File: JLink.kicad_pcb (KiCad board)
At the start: 2 copper layers, 1 part

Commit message: 20250630
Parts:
- added C1: ~, kicad_community_lib:CL10C200JB81PNC, F.Cu at (157.5, 57.7)
- added C10: 4.7uf, kicad_community_lib:CC0603KRX5R8BB475, F.Cu at (143.0, 83.2)
- added C11: 100nf, kicad_community_lib:0603B104K101CT, F.Cu at (143.0, 85.5)
- added C12: 4.7uf, kicad_community_lib:CC0603KRX5R8BB475, F.Cu at (143.0, 87.9)
- added C13: ~, kicad_community_lib:0603B105K250NT, F.Cu at (143.0, 90.2)
- added C14: ~, kicad_community_lib:0603B105K250NT, F.Cu at (143.0, 92.6)
- added C2: ~, kicad_community_lib:CL10C200JB81PNC, F.Cu at (157.5, 60.1)
- added C3: 10nf, kicad_community_lib:CC0603KRX7R6BB103, F.Cu at (121.0, 82.1)
- added C4: ~, kicad_community_lib:CC0603KRX7R6BB103, F.Cu at (121.0, 84.5)
- added C5: ~, kicad_community_lib:CC0603KRX7R6BB103, F.Cu at (121.0, 86.9)
- added C6: ~, kicad_community_lib:CC0603KRX7R6BB103, F.Cu at (121.0, 89.2)
- added C7: 100nf, kicad_community_lib:0603B104K101CT, F.Cu at (136.8, 57.7)
- added C8: 100nf, kicad_community_lib:0603B104K101CT, F.Cu at (136.8, 60.1)
- added C9: 100nf, kicad_community_lib:0603B104K101CT, F.Cu at (143.0, 80.8)
- added CN1: ~, kicad_community_lib:A2541WV-2x4P, F.Cu at (146.7, 74.3)
- added D1: ~, kicad_community_lib:PRTR5V0U2X__NXP Semiconductors, F.Cu at (136.7, 63.5)
- added LDO1: ~, kicad_community_lib:ME6211C33M5G-N, F.Cu at (146.8, 89.4)
- added R1: ~, kicad_community_lib:RTT03512JTP, F.Cu at (121.0, 57.7)
- added R2: ~, kicad_community_lib:RTT03512JTP, F.Cu at (121.0, 60.1)
- added R3: ~, kicad_community_lib:RC0603FR-0724RL, F.Cu at (121.0, 62.4)
- added R4: ~, kicad_community_lib:RC0603FR-0724RL, F.Cu at (121.0, 64.8)
- added R5: ~, kicad_community_lib:RC0603FR-0724RL, F.Cu at (121.0, 67.2)
- added R6: ~, kicad_community_lib:RC0603FR-0724RL, F.Cu at (121.0, 69.5)
- added RN1: 10K, kicad_community_lib:4D03WGJ0472T5E, F.Cu at (139.0, 67.2)
- added RN2: 10K, kicad_community_lib:4D03WGJ0472T5E, F.Cu at (125.0, 87.0)
- added U2: ~, kicad_community_lib:STM32F205RET6, F.Cu at (148.0, 63.8)
- added U3: ~, kicad_community_lib:B0505S-1W__Rlt, F.Cu at (151.2, 85.5)
- added USB1: TYPE-C 16P CB0.8 073, Connect:USB-C-SMD_TYPE-C-16P-CB0.8-073, F.Cu at (129.4, 73.6)
- added X1: ~, Oscillator:CRYSTAL-SMD_4P-L3.2-W2.5-BL, F.Cu at (155.4, 73.2)
- U1: footprint IC:QFP50P1600X1600X160-100N -> kicad_community_lib:ADUM3160BRWZ-RL
- moved U1 28.4 mm to (128.6, 63.0)
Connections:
- U1 pad 1: unconnected-(U1-PE2-Pad1) -> P5VP
- U1 pad 10: Net-(U1-VSS-Pad10) -> Net-(U1-DD+)
- U1 pad 11: Net-(U1-VDD-Pad100) -> Net-(U1-DD-)
- U1 pad 12: unconnected-(U1-PH0_OSC_IN-Pad12) -> /USB/VDD2
- U1 pad 13: unconnected-(U1-PH1_OSC_OUT-Pad13) -> /USB/VDD2
- U1 pad 14: unconnected-(U1-NRST-Pad14) -> /USB/VDD2
- U1 pad 15: unconnected-(U1-PC0-Pad15) -> GND
- U1 pad 16: unconnected-(U1-PC1-Pad16) -> /USB/P5V
- U1 pad 2: unconnected-(U1-PE3-Pad2) -> PGND
- U1 pad 3: unconnected-(U1-PE4-Pad3) -> /USB/VDD1
- U1 pad 4: unconnected-(U1-PE5-Pad4) -> /USB/VDD1
- U1 pad 5: unconnected-(U1-PE6-Pad5) -> /USB/VDD1
- U1 pad 6: unconnected-(U1-VBAT-Pad6) -> Net-(U1-UD–)
- U1 pad 7: unconnected-(U1-PC13-Pad7) -> Net-(U1-UD+)
- U1 pad 8: unconnected-(U1-PC14_OSC32_IN-Pad8) -> PGND
- U1 pad 9: unconnected-(U1-PC15_OSC32_OUT-Pad9) -> GND

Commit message: 基本完成
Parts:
- added C15: ~, kicad_community_lib:CL10B104KC8NNNC, F.Cu at (86.8, 86.8)
- added C16: ~, kicad_community_lib:CL10B104KC8NNNC, F.Cu at (86.8, 82.8)
- added C17: ~, kicad_community_lib:CL10B104KC8NNNC, F.Cu at (86.8, 78.8)
- added C18: ~, kicad_community_lib:CL10B104KC8NNNC, F.Cu at (86.8, 74.8)
- added C19: ~, kicad_community_lib:CL10B104KC8NNNC, F.Cu at (86.7, 70.8)
- added C20: ~, kicad_community_lib:CL10B104KC8NNNC, F.Cu at (86.8, 66.8)
- added C21: ~, kicad_community_lib:CL10B104KC8NNNC, F.Cu at (86.8, 62.8)
- added C22: ~, kicad_community_lib:CL10B104KC8NNNC, F.Cu at (89.5, 66.8)
- added C23: ~, kicad_community_lib:CL10B104KC8NNNC, F.Cu at (89.5, 62.8)
- added C24: ~, kicad_community_lib:CL10B104KC8NNNC, F.Cu at (89.5, 70.8)
- added C25: ~, kicad_community_lib:CL10B104KC8NNNC, F.Cu at (89.5, 86.8)
- added C26: ~, kicad_community_lib:CL10B104KC8NNNC, F.Cu at (89.5, 82.8)
- added C27: ~, kicad_community_lib:CL10B104KC8NNNC, F.Cu at (89.5, 78.8)
- added C28: ~, kicad_community_lib:CL10B104KC8NNNC, F.Cu at (89.5, 74.8)
- added C29: ~, kicad_community_lib:0603B225K250NT, F.Cu at (77.4, 72.0)
- added C30: ~, kicad_community_lib:0603B225K250NT, B.Cu at (65.5, 72.6)
- added C31: ~, kicad_community_lib:0603B225K250NT, B.Cu at (64.2, 72.6)
- added C32: ~, kicad_community_lib:0603B225K250NT, B.Cu at (67.5, 78.6)
- added C33: ~, kicad_community_lib:0603B225K250NT, F.Cu at (63.5, 83.8)
- added C34: ~, kicad_community_lib:0603B225K250NT, B.Cu at (71.2, 71.8)
- added C35: ~, kicad_community_lib:0603B225K250NT, B.Cu at (70.0, 79.3)
- added C36: ~, kicad_community_lib:0603B225K250NT, B.Cu at (71.2, 78.1)
- added D2: ~, kicad_community_lib:MBR0530__YANGJIE, F.Cu at (69.9, 66.0)
- added D3: ~, kicad_community_lib:MBR0530__YANGJIE, F.Cu at (58.4, 66.2)
- added H1: ~, Connect:PZ200-2-10-Z, F.Cu at (97.9, 75.5)
- added LED1: ~, kicad_community_lib:SZYY0603RB2, F.Cu at (80.4, 71.5)
- added Q1: ~, kicad_community_lib:SS8050__SHIKUES, F.Cu at (76.9, 86.8)
- added Q2: ~, kicad_community_lib:SS8550 Y2, F.Cu at (77.9, 83.0)
- added R7: ~, kicad_community_lib:RK73Z1JTTD, F.Cu at (75.1, 82.5)
- added RN10: 100 Ohm, kicad_community_lib:YC164-FR-07100RL, F.Cu at (93.5, 85.8)
- added RN11: 220K, kicad_community_lib:4D03WGJ0224T5E, F.Cu at (93.3, 77.4)
- added RN3: 10K, kicad_community_lib:4D03WGJ0472T5E, F.Cu at (80.4, 67.8)
- added RN4: 220K, kicad_community_lib:4D03WGJ0224T5E, F.Cu at (93.3, 73.6)
- added RN5: 470Ω, kicad_community_lib:4D03WGJ0471T5E, F.Cu at (93.3, 66.2)
- added RN6: 470Ω, kicad_community_lib:4D03WGJ0471T5E, F.Cu at (93.5, 81.5)
- added RN7: ~, kicad_community_lib:YC164-FR-07100RL, F.Cu at (93.3, 69.9)
- added RN8: 470Ω, kicad_community_lib:4D03WGJ0471T5E, F.Cu at (82.4, 74.8)
- added RN9: 470Ω, kicad_community_lib:4D03WGJ0471T5E, F.Cu at (82.4, 78.8)
- added U10: ~, kicad_community_lib:SN74LVC2T45DCUR, F.Cu at (88.0, 84.8)
- added U11: ~, kicad_community_lib:SN74LVC2T45DCUR, F.Cu at (88.0, 88.8)
- added U4: ~, kicad_community_lib:SN74LVC2T45DCUR, F.Cu at (88.0, 64.8)
- added U5: ~, kicad_community_lib:SN74LVC2T45DCUR, F.Cu at (88.0, 68.8)
- added U6: ~, kicad_community_lib:SN74LVC2T45DCUR, F.Cu at (88.0, 80.8)
- added U7: ~, kicad_community_lib:MCP6002T-I_SN, F.Cu at (64.1, 64.8)
- added U8: ~, kicad_community_lib:SN74LVC2T45DCUR, F.Cu at (88.0, 72.8)
- added U9: ~, kicad_community_lib:SN74LVC2T45DCUR, F.Cu at (88.0, 76.8)
- R3, R4: value ~ -> 24Ω
- moved U3 102.3 mm to (50.6, 66.8)
- moved D1 97.3 mm to (41.5, 83.8), turned to 90 degrees
- moved C9 97.1 mm to (46.6, 69.0), turned to 180 degrees
- moved C1 95.8 mm to (65.5, 84.5), turned to 180 degrees
- moved C10 94.7 mm to (49.4, 69.0), turned to 180 degrees
- moved CN1 92.9 mm to (54.5, 85.8), turned to 180 degrees
- moved C8 92.8 mm to (44.7, 72.0), turned to 90 degrees
- moved C2 92.6 mm to (68.2, 84.5), turned to 180 degrees
- moved C11 91.6 mm to (52.9, 69.0), turned to 180 degrees
- moved USB1 89.9 mm to (39.5, 75.2), turned to -90 degrees
- moved X1 89.8 mm to (66.7, 87.3), turned to 180 degrees
- moved C12 89.6 mm to (55.4, 69.0)
- moved R2 86.0 mm to (38.3, 83.2), turned to 180 degrees
- moved R1 83.2 mm to (38.5, 67.8), turned to 180 degrees
- moved U2 80.7 mm to (68.1, 75.5), turned to 90 degrees
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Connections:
- net /Connect/TIMA renamed TIMA
- net /STM32/JTCK_SWCK renamed JTCK_SWCK
- net /STM32/JTCK_SWDIO renamed JTCK_SWDIO
- net /STM32/JTDI renamed JTDI
- net /STM32/JTDO_SWO renamed JTDO_SWO
- net /STM32/JTRST renamed JTRST
- R3 pad 1: /USB/PDD_P -> /PDDP
- R4 pad 1: /USB/PDD_N -> /PDDM
- RN2 pad 1: /Connect/PADC1 -> /ADC4
- RN2 pad 2: /Connect/PADC2 -> /ADC3
- RN2 pad 3: /Connect/PADC3 -> /ADC2
- RN2 pad 4: /Connect/PADC4 -> /ADC1
- RN2 pad 5: /Connect/VEE -> VEE
- RN2 pad 7: /Connect/P5V -> P5V
- RN2 pad 8: /Connect/EPWR -> EPWR
- U2 pad 10: unconnected-(U2-PC2-Pad10) -> NCTL1
- U2 pad 15: unconnected-(U2-PA1-Pad15) -> NTCL2
- U2 pad 16: unconnected-(U2-PA2-Pad16) -> NTCL3
- U2 pad 17: unconnected-(U2-PA3-Pad17) -> NTCL4
- U2 pad 21: unconnected-(U2-PA5-Pad21) -> NDAT8
- U2 pad 22: unconnected-(U2-PA6-Pad22) -> NDAT7
- U2 pad 23: unconnected-(U2-PA7-Pad23) -> NDAT3
- U2 pad 25: unconnected-(U2-PC5-Pad25) -> NDAT12
- U2 pad 27: unconnected-(U2-PB1-Pad27) -> NDAT9
- U2 pad 28: unconnected-(U2-PB2-Pad28) -> NDAT10
- U2 pad 29: unconnected-(U2-PB10-Pad29) -> PLED2
- U2 pad 30: unconnected-(U2-PB11-Pad30) -> PLED1
- U2 pad 31: unconnected-(U2-VCAP_1-Pad31) -> VCAP1
- U2 pad 33: unconnected-(U2-PB12-Pad33) -> NDAT9
- U2 pad 34: unconnected-(U2-PB13-Pad34) -> NDAT8
- U2 pad 35: unconnected-(U2-PB14-Pad35) -> NDAT6
- U2 pad 36: unconnected-(U2-PB15-Pad36) -> NDAT11
- U2 pad 37: unconnected-(U2-PC6-Pad37) -> NDAT8
- U2 pad 38: unconnected-(U2-PC7-Pad38) -> NDAT11
- U2 pad 39: unconnected-(U2-PC8-Pad39) -> NDAT5
- U2 pad 40: unconnected-(U2-PC9-Pad40) -> NDAT4
- U2 pad 41: unconnected-(U2-PA8-Pad41) -> NDAT2
- U2 pad 43: unconnected-(U2-PA10-Pad43) -> NDAT1
- U2 pad 44: unconnected-(U2-PA11-Pad44) -> /PDDM
- U2 pad 45: unconnected-(U2-PA12-Pad45) -> /PDDP
- U2 pad 47: unconnected-(U2-VCAP_2-Pad47) -> VCAP2
- U2 pad 53: unconnected-(U2-PC12-Pad53) -> NDAT11
- U2 pad 59: unconnected-(U2-PB7-Pad59) -> NPWR
- U2 pad 60: unconnected-(U2-BOOT0-Pad60) -> GND
- U2 pad 61: unconnected-(U2-PB8-Pad61) -> NSRST
- U2 pad 7: /STM32/NRST -> NRESET

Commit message: 修改内容中
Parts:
- C31: moved to F.Cu
- moved R6 5.78 mm to (47.3, 82.2), turned to 180 degrees
- moved RN10 4.60 mm to (93.3, 81.2)
- moved R5 4.49 mm to (47.3, 83.4), turned to 180 degrees
- moved C31 3.58 mm to (62.4, 69.5), turned to 180 degrees
- moved RN6 3.42 mm to (93.3, 84.9)
- moved R3 3.30 mm to (60.1, 75.7), turned to -90 degrees
- moved CN1 3.00 mm to (56.6, 87.9)
- moved D1 2.35 mm to (43.6, 82.7), turned to 180 degrees
- moved R4 2.21 mm to (58.8, 75.7), turned to -90 degrees
- moved Q2 0.78 mm to (78.5, 82.5)
- moved C35 0.76 mm to (70.1, 78.6), turned to 90 degrees
- moved Q1 0.76 mm to (77.0, 87.5), turned to 0 degrees
- moved USB1 0.65 mm to (38.9, 75.2)
- moved C36 0.50 mm to (71.5, 77.7), turned to 90 degrees
- moved LED1 0.48 mm to (80.8, 71.3), turned to 90 degrees
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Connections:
- net /PDDM renamed /PDDN
- net Net-(U1-DD+) renamed /USB/DD+
- net Net-(U1-DD-) renamed /USB/DD-
- net Net-(U1-UD+) renamed /USB/UD+
- net Net-(U1-UD–) renamed /USB/UD-
- C7 pad 2: /USB/P5V -> P5V
- CN1 pad 6: /STM32/JTMS_SWDIO -> JTCK_SWDIO
- RN10 pad 5: Net-(U10-B1) -> Net-(Q1-Pad2)
- RN10 pad 6: Net-(U10-B2) -> Net-(Q1-Pad2)
- RN10 pad 7: Net-(Q1-Pad2) -> Net-(U10-B2)
- RN10 pad 8: Net-(Q1-Pad2) -> Net-(U10-B1)
- RN3 pad 5: TVRF -> Net-(Q2-B)
- RN3 pad 6: ENSRST -> 3V3
- RN3 pad 7: 3V3 -> ENSRST
- RN3 pad 8: Net-(Q2-B) -> TVRF
- U1 pad 16: /USB/P5V -> P5V
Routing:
- net TVRF: track 0.00 -> 49.9 mm, vias 0 -> 2
- net NDAT11: track 0.00 -> 41.3 mm, vias 0 -> 2
- net ENSRST: track 0.00 -> 31.0 mm, vias 0 -> 3
- net Net-(Q2-B): track 0.00 -> 30.1 mm
- net JTCK_SWDIO: track 0.00 -> 29.8 mm, vias 0 -> 1
- net Net-(Q1-Pad2): track 0.00 -> 27.8 mm
- net ETCK: track 0.00 -> 26.8 mm
- net JTDI: track 0.00 -> 22.9 mm, vias 0 -> 1
- net NDAT12: track 0.00 -> 22.1 mm, vias 0 -> 2
- net Net-(U7-+INA): track 0.00 -> 21.9 mm
- net Net-(Q1-Pad1): track 0.00 -> 21.4 mm
- net /ADC3: track 0.00 -> 21.0 mm, vias 0 -> 2
- net /ADC1: track 0.00 -> 20.5 mm, vias 0 -> 2
- net /ADC2: track 0.00 -> 20.0 mm, vias 0 -> 2
- net /ADC4: track 0.00 -> 19.6 mm, vias 0 -> 2
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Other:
- board outline added: 75 x 35 mm
- copper layers 2 -> 4

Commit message: JLINK will complite
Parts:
- added C37: 100nf, kicad_community_lib:0603B104K101CT, F.Cu at (44.7, 75.2)
- added C38: 100nf, kicad_community_lib:0603B104K101CT, F.Cu at (59.4, 71.8)
- moved C7 2.75 mm to (58.2, 69.5), turned to 180 degrees
- moved R7 1.09 mm to (75.2, 81.4), turned to 0 degrees
- moved RN1 0.49 mm to (77.9, 75.1)
- moved RN2 0.46 mm to (77.9, 78.3)
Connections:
- CN1 pad 6: JTCK_SWDIO -> /STM32/JTMS_SWDIO
- Q2 pad 2: Net-(Q2-E) -> TIMA
- R7 pad 2: Net-(Q2-E) -> TIMA
- U2 pad 15: NTCL2 -> NCTL2
- U2 pad 16: NTCL3 -> NCTL3
- U2 pad 17: NTCL4 -> NCTL4
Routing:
- net NPWR: track 0.00 -> 49.5 mm, vias 0 -> 2
- net NSRST: track 0.00 -> 46.9 mm, vias 0 -> 2
- net NCTL1: track 0.00 -> 33.8 mm, vias 0 -> 2
- net EPWR: track 2.70 -> 29.3 mm, vias 0 -> 2
- net NCTL3: track 0.00 -> 25.1 mm, vias 0 -> 2
- net NCTL2: track 0.00 -> 23.4 mm, vias 0 -> 2
- net NDAT2: track 0.00 -> 23.3 mm, vias 0 -> 2
- net NDAT1: track 0.00 -> 22.5 mm, vias 0 -> 2
- net NDAT4: track 0.00 -> 20.7 mm, vias 0 -> 2
- net Net-(Q2-B): track 30.1 -> 48.2 mm, vias 0 -> 2
- net NCTL4: track 0.00 -> 17.4 mm, vias 0 -> 2
- net NDAT10: track 0.00 -> 16.0 mm, vias 0 -> 2
- net NDAT11: track 41.3 -> 55.1 mm
- net NDAT8: track 8.13 -> 20.6 mm
- net /USB/USB_P: track 0.00 -> 12.2 mm
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
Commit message: 2025/07/25
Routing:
- net TVRF: track 49.9 -> 48.6 mm
- net Net-(U6-A2): track 8.53 -> 9.14 mm
- net PGND: vias 6 -> 8

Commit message: 覆铜
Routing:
- net Net-(USB1-CC2): track 9.55 -> 8.48 mm
- net /USB/UD+: track 10.9 -> 11.8 mm
- net /USB/UD-: track 9.94 -> 10.7 mm
- net /USB/VDD2: track 12.0 -> 12.5 mm
- added copper zone on B.Cu, net PGND
- added copper zone on F.Cu, net PGND

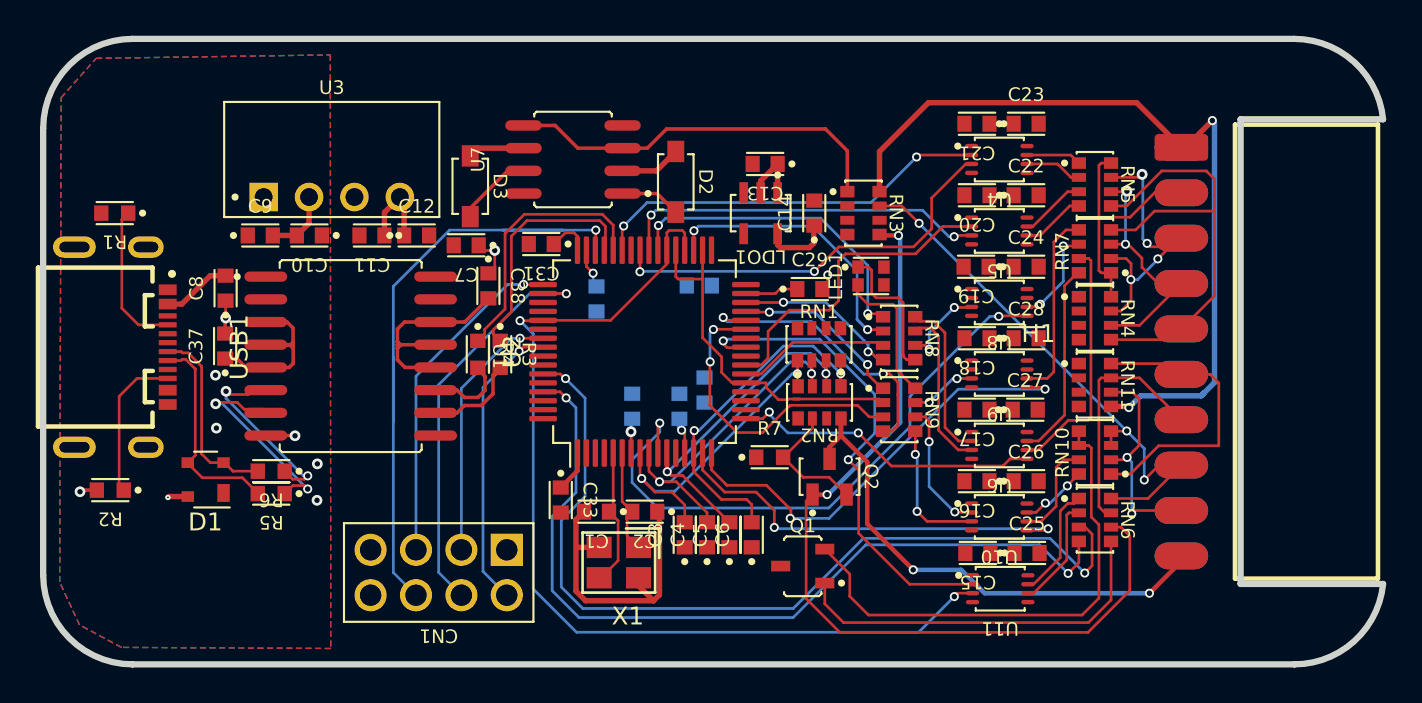
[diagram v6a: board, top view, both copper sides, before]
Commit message: 添加覆铜GND和PGND
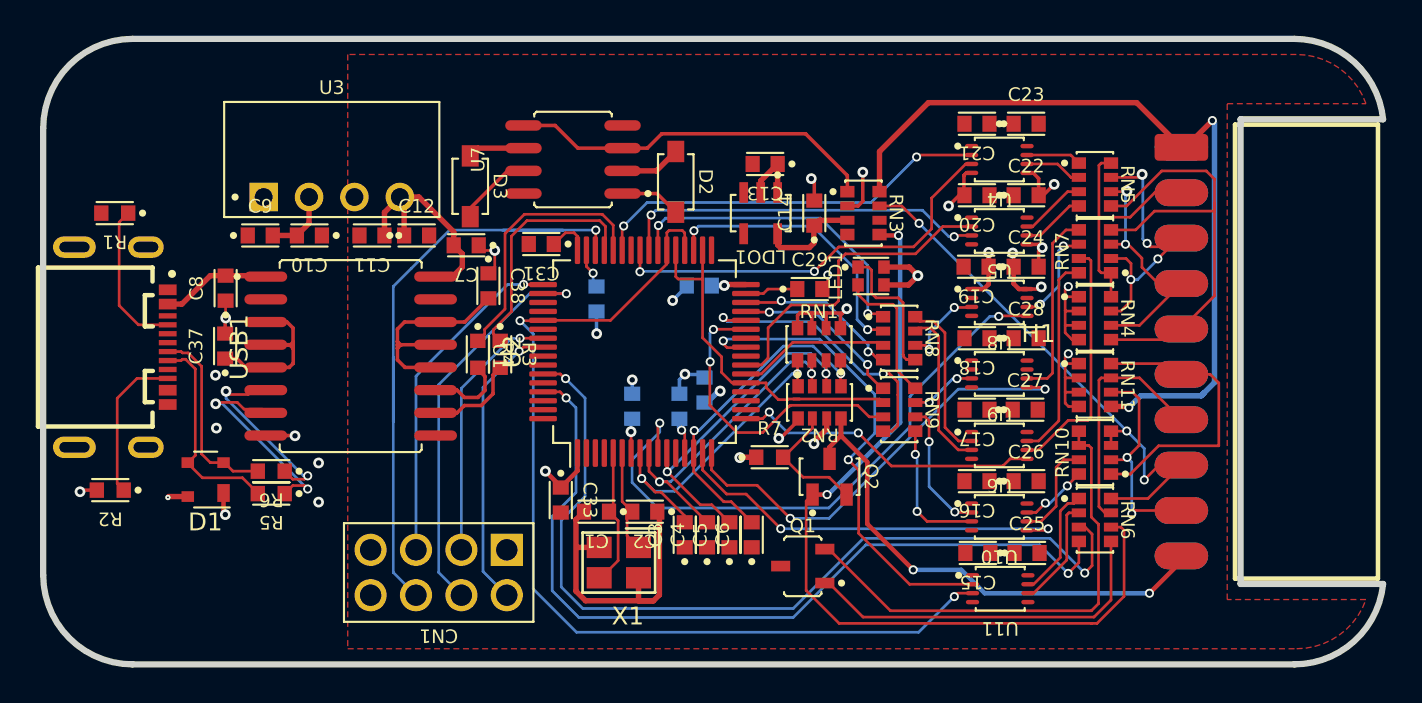
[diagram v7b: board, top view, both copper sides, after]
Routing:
- net GND: track 20.0 -> 53.5 mm, vias 2 -> 13
- net P3V3: track 10.5 -> 23.9 mm, vias 1 -> 6
- net P5V: track 8.00 -> 18.3 mm, vias 0 -> 2
- net VEE: track 6.59 -> 14.3 mm, vias 0 -> 4
- net P5VP: track 8.81 -> 11.1 mm
- net PGND: track 4.46 -> 5.71 mm, vias 8 -> 9
- net Net-(U7-+INA): track 21.9 -> 20.9 mm
- net Net-(Q2-B): track 48.2 -> 47.3 mm
- net Net-(Q1-Pad1): track 21.4 -> 20.5 mm
- net Net-(Q1-Pad2): track 28.1 -> 27.3 mm
- net /ADC4: track 19.6 -> 19.0 mm
- net NCTL2: track 23.4 -> 22.9 mm
- added copper zone on F.Cu, net GND
- removed copper zone on B.Cu, net PGND

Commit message: 20250807基本完成，只剩下检查
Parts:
- moved R7 0.76 mm to (75.1, 82.2)
- moved C14 0.68 mm to (77.0, 67.8)
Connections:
- CN1 pad 6: /STM32/JTMS_SWDIO -> JTCK_SWDIO
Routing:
- net P3V3: track 23.9 -> 159.0 mm, vias 6 -> 15
- net VEE: track 14.3 -> 100.5 mm, vias 4 -> 13
- net P5V: track 18.3 -> 73.4 mm, vias 2 -> 5
- net GND: track 53.5 -> 95.9 mm, vias 13 -> 42
- net 3V3: track 0.00 -> 25.7 mm, vias 0 -> 2
- net P5VP: track 11.1 -> 32.2 mm
- net PGND: track 5.71 -> 9.82 mm, vias 9 -> 12
- net TVRF: track 48.6 -> 50.8 mm
- net ENSRST: track 29.8 -> 31.5 mm
- net NDAT9: track 17.4 -> 18.5 mm
- net NCTL1: track 33.8 -> 34.6 mm
- added copper zone on B.Cu, net GND
- added copper zone on In1.Cu, net GND
- added copper zone on F.Cu, net P3V3
- added copper zone on F.Cu, net P5VP
- added copper zone on B.Cu, net PGND
- added copper zone on In1.Cu, net PGND
